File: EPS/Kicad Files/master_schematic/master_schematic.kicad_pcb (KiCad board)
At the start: 2 copper layers, 96 x 90 mm, 79 parts, among them J1 USB_C_Receptacle, J2 436500212, J3 Conn_02x20_Odd_Even, J4 Conn_01x05_Female, Q1 FZT688BTA, Q2 FZT688BTA, U1 RPM5.0-2.0, U2 RPM5.0-2.0, U3 RPM3.3-2.0, U4 INA3221, U5 MAX77757JEFG435+, U6 MAX17055EWL+T, U7 ATA6560-GAQW-VAO, U8 PIC18F27Q84-E/SP

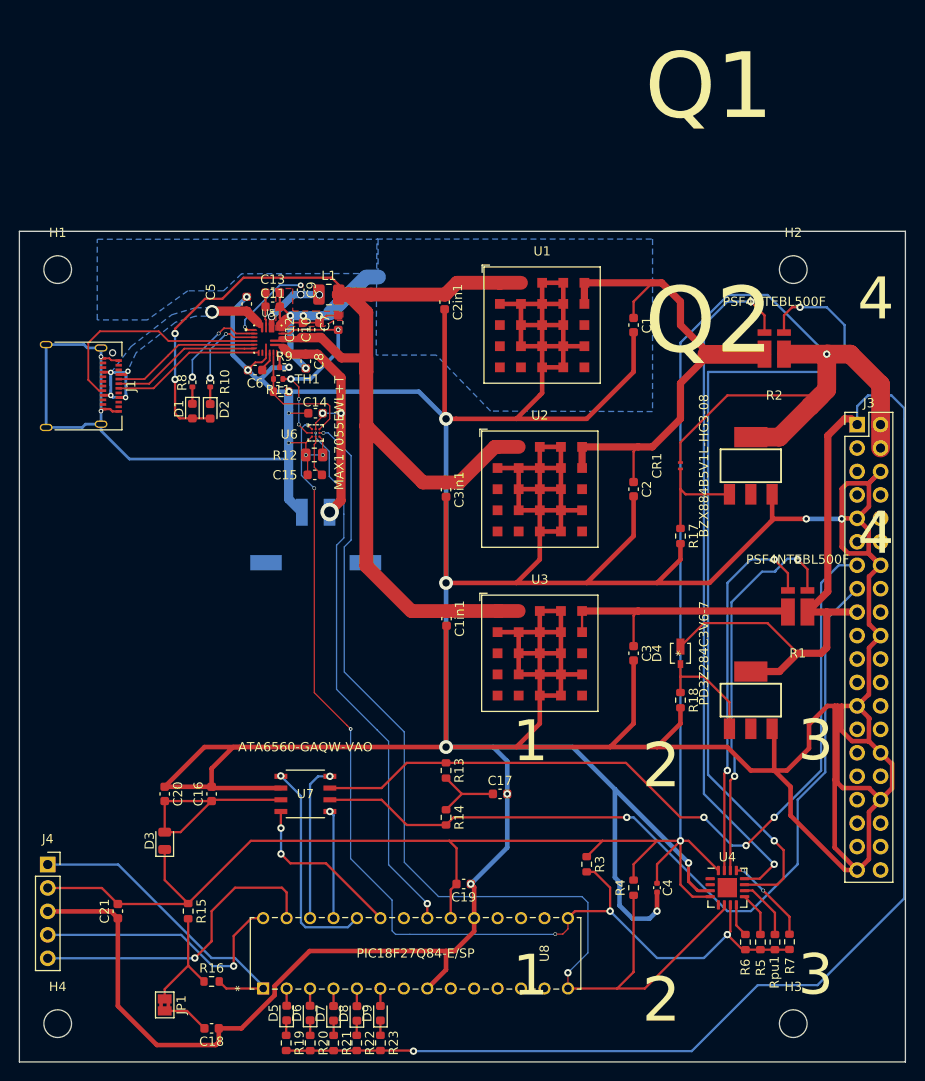
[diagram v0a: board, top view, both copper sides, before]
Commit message: eps pcb update
all errors and warnings corrected
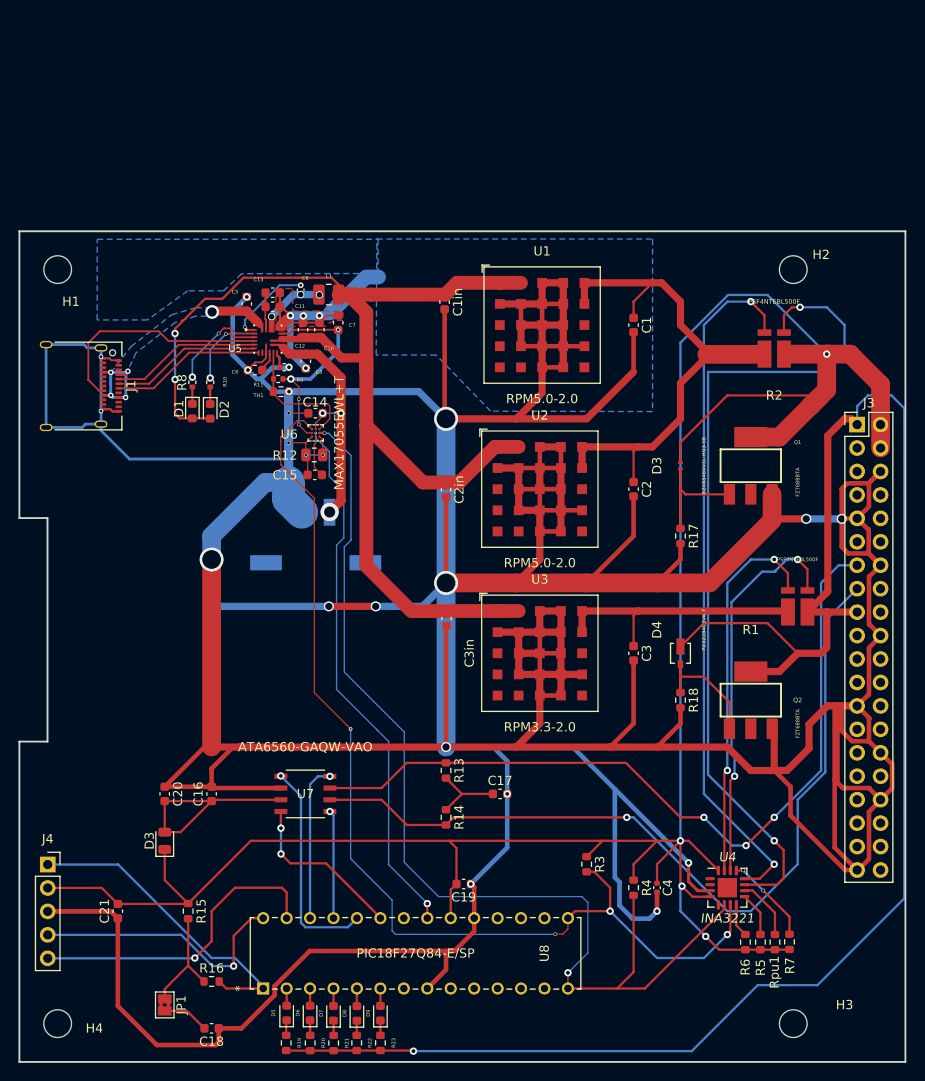
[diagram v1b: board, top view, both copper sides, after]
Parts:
- turned R4 to -90 degrees
- renumbered C2in1 to C1in, C3in1 to C2in, C1in1 to C3in, CR1 to D3
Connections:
- R3 pad 2: /ColoradoCUBE_Payload/5V -> /ColoradoCUBE_Payload/SDA_RC4
- R4 pad 2: /ColoradoCUBE_Payload/5V -> /ColoradoCUBE_Payload/SCL_RC3
- U4 pad 6: /ColoradoCUBE_Payload/5V -> /ColoradoCUBE_Payload/SCL_RC3
- U4 pad 7: /ColoradoCUBE_Payload/5V -> /ColoradoCUBE_Payload/SDA_RC4
- U6 pad A2: /ColoradoCUBE_Payload/5V -> /ColoradoCUBE_Payload/SCL_RC3
- U6 pad C1: /ColoradoCUBE_Payload/5V -> /ColoradoCUBE_Payload/SDA_RC4
- U8 pad 14: /ColoradoCUBE_Payload/5V -> /ColoradoCUBE_Payload/SCL_RC3
- U8 pad 15: /ColoradoCUBE_Payload/5V -> /ColoradoCUBE_Payload/SDA_RC4
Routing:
- net /ColoradoCUBE_Payload/5V: track 479.1 -> 262.2 mm, vias 10 -> 4
- net /ColoradoCUBE_Payload/SCL_RC3: track 0.00 -> 115.2 mm, vias 0 -> 2
- net /ColoradoCUBE_Payload/SDA_RC4: track 0.00 -> 113.5 mm, vias 0 -> 4
- net GND: track 834.1 -> 901.5 mm, vias 19 -> 22
- net Net-(C9-Pad2): track 8.04 -> 7.10 mm
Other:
- outline, holes or cut-outs redrawn

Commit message: Eps board update
vias fixed for manufacturers standards, eliminated ALRT pin on battery gauge
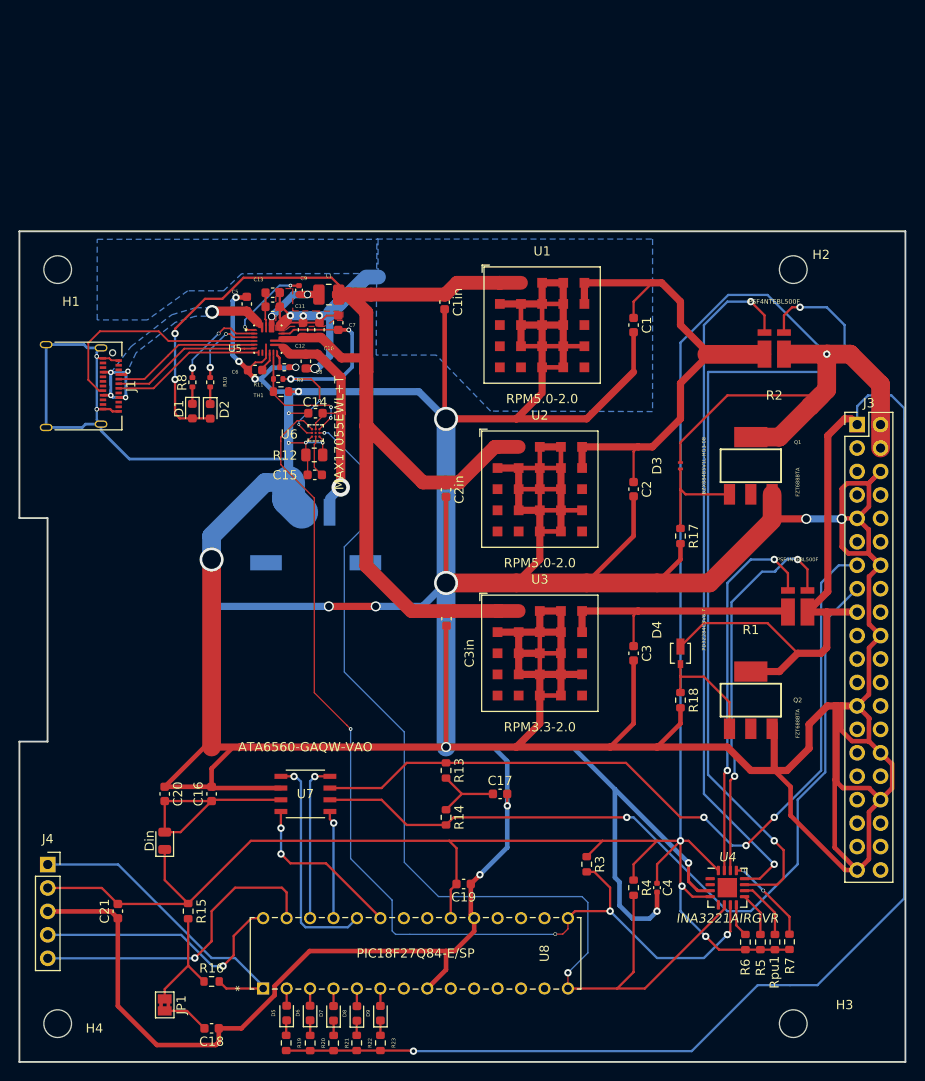
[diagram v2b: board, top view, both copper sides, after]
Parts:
- U4: value INA3221 -> INA3221AIRGVR
- moved C9 0.18 mm to (67.9, 62.2)
- renumbered D3 to Din
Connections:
- U6 pad B2: ALRT -> unconnected-(U6-PadB2)
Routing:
- net ALRT: track 58.2 -> 0.00 mm, vias 2 -> 0
- net Net-(C7-Pad1): track 22.5 -> 29.7 mm
- net GND: track 901.5 -> 907.2 mm, vias 22 -> 23
- net GNDPWR: track 29.2 -> 30.3 mm
- net /ColoradoCUBE_Payload/SCL_RC3: track 115.2 -> 116.2 mm
- net Net-(C9-Pad2): track 7.10 -> 7.96 mm, vias 3 -> 2
- net /ColoradoCUBE_Payload/CAN_Transceiver/CAN_TX: track 23.5 -> 24.4 mm
- net /ColoradoCUBE_Payload/ICSPD: track 28.8 -> 28.1 mm
- net /charge schem/V_BAT: vias 3 -> 1
- net Net-(R11-Pad2): vias 0 -> 2

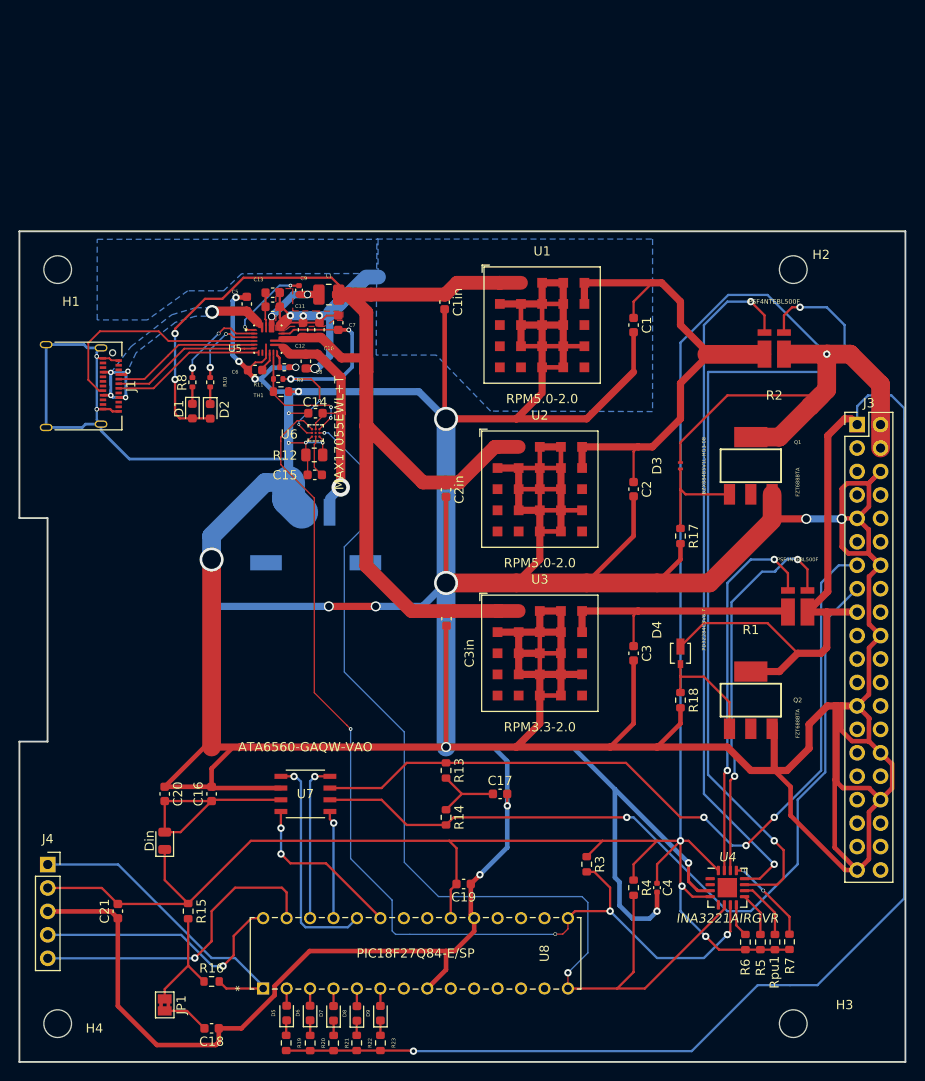
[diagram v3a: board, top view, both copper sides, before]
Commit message: eps redesign
updated boost converter
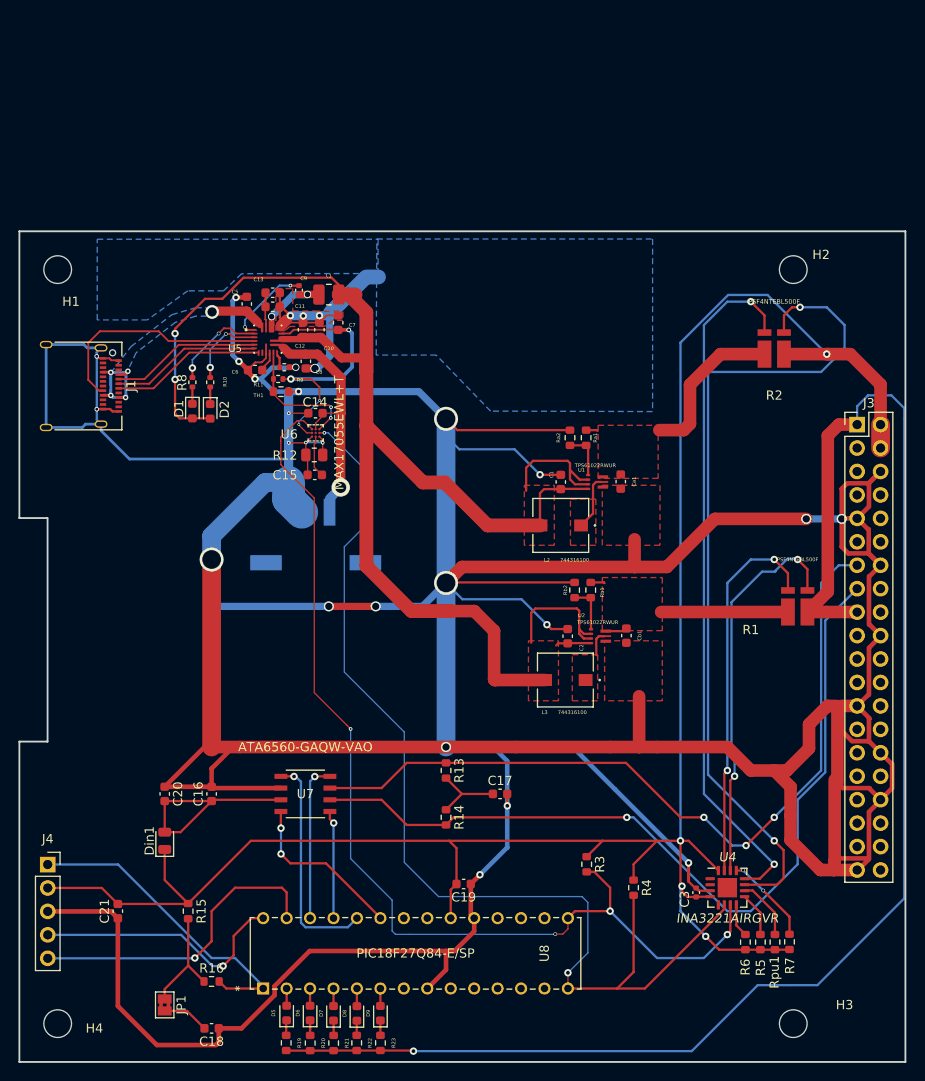
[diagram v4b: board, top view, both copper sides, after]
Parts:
- removed C1in, C2in, C3in: 20μF, Capacitor_SMD:C_0603_1608Metric
- removed the C3 at (104.1, 101.6)
- removed D3: BZX884B5V1L-HG3-08, hg3-08:BZX884B5V1L-HG3-08
- removed D4: PD3Z284C3V6-7, PD3z284:PD3Z284C3V6-7
- removed Q1, Q2: FZT688BTA, fzt:SOT230P700X180-4N
- removed R17, R18: 1k, Resistor_SMD:R_0603_1608Metric
- removed U3: RPM3.3-2.0, Converter_DCDC:Converter_DCDC_RECOM_RPMx.x-x.0
- added Ca1: 22uF, Capacitor_SMD:C_0603_1608Metric, F.Cu at (102.8, 83.0)
- added Cb1: 5uF, Capacitor_SMD:C_0603_1608Metric, F.Cu at (103.4, 99.7)
- added L2: 744316100, footprints1:744316100, F.Cu at (96.2, 87.8)
- added L3: 744316100, footprints1:744316100, F.Cu at (96.8, 104.5)
- added Ra1: 732K, Resistor_SMD:R_0603_1608Metric, F.Cu at (99.0, 78.2)
- added Ra2: 100k, Resistor_SMD:R_0603_1608Metric, F.Cu at (97.2, 78.2)
- added Rb1: 450k, Resistor_SMD:R_0603_1608Metric, F.Cu at (99.5, 94.8)
- added Rb2: 100k, Resistor_SMD:R_0603_1608Metric, F.Cu at (97.8, 94.8)
- C1, C2: value 20μF -> 10uF
- U1, U2: value RPM5.0-2.0 -> TPS61022RWUR; footprint Converter_DCDC:Converter_DCDC_RECOM_RPMx.x-x.0 -> footprints:TPS61022RWUR
- moved C1 18.7 mm to (96.2, 83.0), turned to 90 degrees
- moved U1 18.0 mm to (100.2, 83.0), turned to 180 degrees
- moved C2 17.5 mm to (97.0, 99.8), turned to 90 degrees
- moved U2 17.2 mm to (100.5, 99.8), turned to 180 degrees
- moved C3 4.28 mm to (110.9, 127.5), turned to 90 degrees
- renumbered C4 to C3, Din to Din1
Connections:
- C1 pad 1: Net-(C1-Pad1) -> /charge schem/SYSPOWER
- C2 pad 1: Net-(C1-Pad1) -> /charge schem/SYSPOWER
- R1 pad 1: Net-(C3-Pad1) -> Net-(Cb1-Pad1)
- R2 pad 1: Net-(C1-Pad1) -> Net-(Ca1-Pad1)
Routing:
- net GND: track 907.2 -> 699.8 mm, vias 23 -> 24
- net Net-(C1-Pad1): track 57.7 -> 0.00 mm
- net /ColoradoCUBE_Payload/5V: track 262.2 -> 220.6 mm
- net /charge schem/SYSPOWER: track 137.3 -> 171.7 mm
- net /ColoradoCUBE_Payload/3.3V: track 193.0 -> 164.2 mm
- net Net-(C3-Pad1): track 28.7 -> 0.00 mm
- net Net-(Ca1-Pad1): track 0.00 -> 18.8 mm
- net Net-(Cb1-Pad1): track 0.00 -> 17.8 mm
- net Net-(D4-Pad2): track 12.4 -> 0.00 mm
- net Net-(D3-Pad2): track 12.0 -> 0.00 mm
- net Net-(L2-Pad1): track 0.00 -> 5.97 mm
- net Net-(Rb1-Pad2): track 0.00 -> 5.19 mm
- net Net-(Ra1-Pad2): track 0.00 -> 5.05 mm
- net Net-(L3-Pad1): track 0.00 -> 2.76 mm
- added copper zone on F.Cu, net /charge schem/SYSPOWER
- added copper zone on F.Cu, net GND
- added copper zone on F.Cu, net Net-(Ca1-Pad1)
- added copper zone on F.Cu, net Net-(Cb1-Pad1)
- added copper zone on F.Cu, net Net-(L2-Pad1)
- added copper zone on F.Cu, net Net-(L3-Pad1)

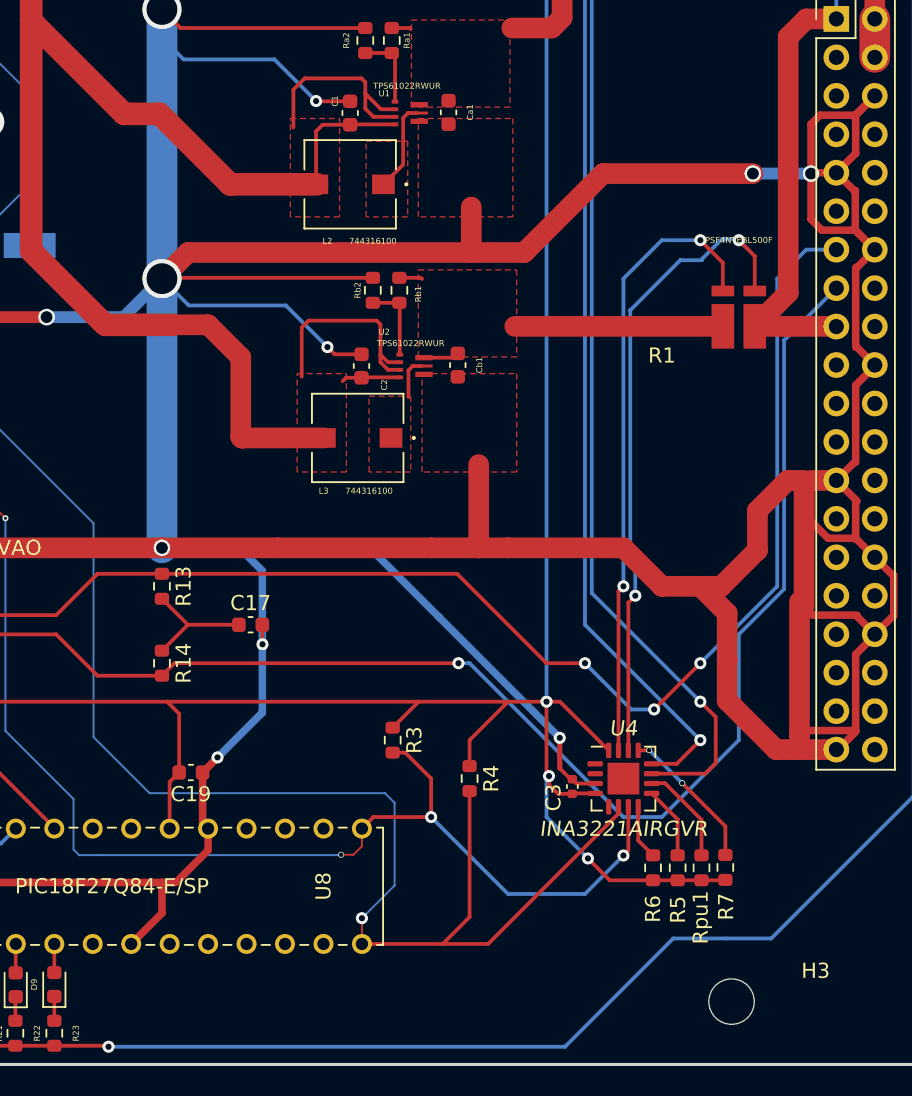
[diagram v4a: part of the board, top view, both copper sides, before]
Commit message: EPS 2.0 update
added alert pins to microcontroller
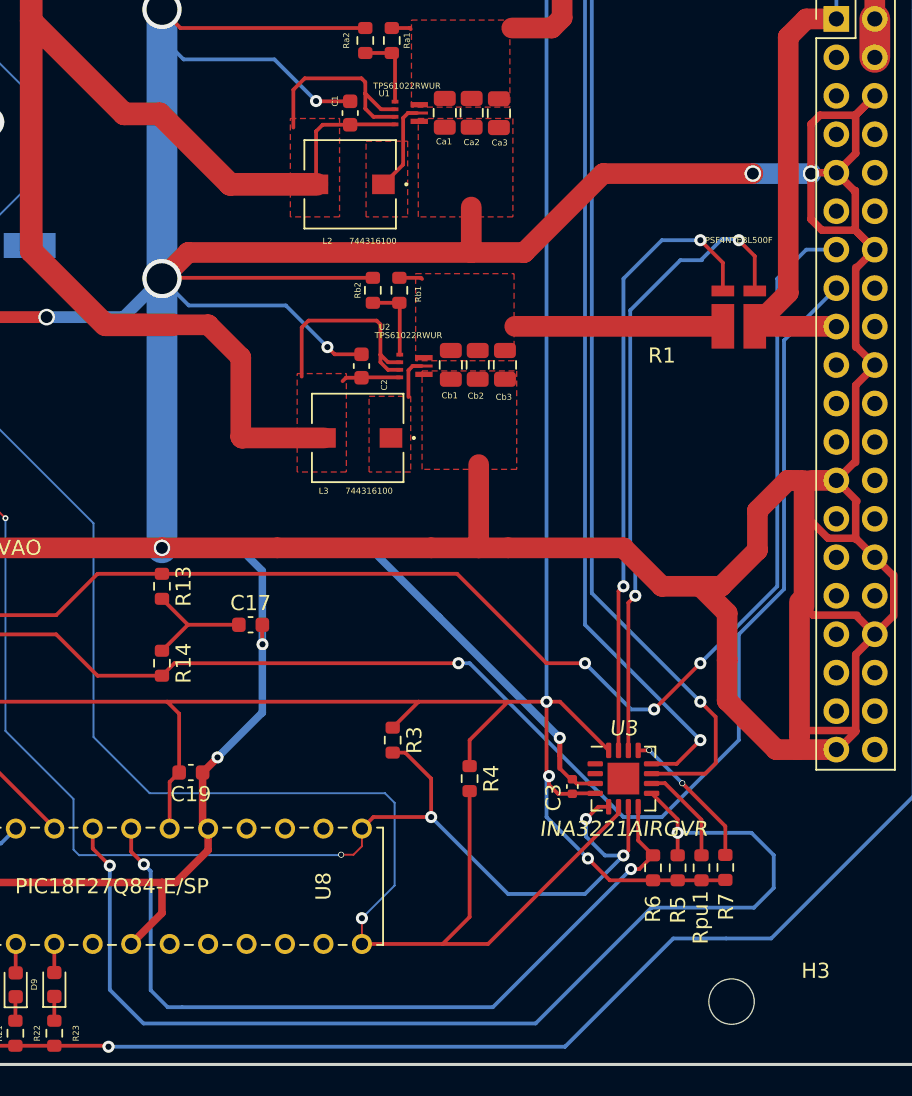
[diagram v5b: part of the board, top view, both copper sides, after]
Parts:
- added Ca2: 22uF, Capacitor_SMD:C_0805_2012Metric, F.Cu at (104.3, 83.0)
- added Ca3: 22uF, Capacitor_SMD:C_0805_2012Metric, F.Cu at (106.1, 83.0)
- added Cb2: 5uF, Capacitor_SMD:C_0805_2012Metric, F.Cu at (104.7, 99.7)
- added Cb3: 5uF, Capacitor_SMD:C_0805_2012Metric, F.Cu at (106.5, 99.7)
- Ca1, Cb1: footprint Capacitor_SMD:C_0603_1608Metric -> Capacitor_SMD:C_0805_2012Metric
- Rb1: value 450k -> 453k
- moved Cb1 0.46 mm to (102.9, 99.7)
- moved Ca1 0.25 mm to (102.5, 83.0)
- renumbered U4 to U3
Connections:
- R5 pad 2: /converterschematic/CRT -> /ColoradoCUBE_Payload/CRT
- R6 pad 2: /converterschematic/WRN -> /ColoradoCUBE_Payload/ALRT
- U3 pad 5: /converterschematic/A0 -> /ColoradoCUBE_Payload/SDA_RC4
- U8 pad 21: ALRT -> /ColoradoCUBE_Payload/ALRT
- U8 pad 22: unconnected-(U8-Pad22) -> /ColoradoCUBE_Payload/CRT
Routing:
- net /ColoradoCUBE_Payload/CRT: track 0.00 -> 73.5 mm, vias 0 -> 2
- net /ColoradoCUBE_Payload/ALRT: track 0.00 -> 52.2 mm, vias 0 -> 2
- net /ColoradoCUBE_Payload/SDA_RC4: track 113.5 -> 119.4 mm, vias 4 -> 5
- net /converterschematic/CRT: track 4.80 -> 0.00 mm
- net /converterschematic/WRN: track 3.61 -> 0.00 mm
- net Net-(Cb1-Pad1): track 17.8 -> 15.4 mm
